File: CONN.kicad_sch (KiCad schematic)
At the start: 21 parts

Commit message: Complete schematics
Nightly update
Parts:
- removed D? (x15): LESD11LL5.0CT5G, 002_GN_TWO-PIN_PLASTIC_SMD:SOD-123, symbol 002_Basic_SingleSemiconductor:007_Diode_ESD_Bi
- added C25: 100nF, 001_GN_RCL_SMD:C0201(0603M), symbol 001_Basic_PassiveComponents:101_Capacitor
- added C26: 1uF, 001_GN_RCL_SMD:C0402(1005M), symbol 001_Basic_PassiveComponents:101_Capacitor
- added D10, D11, D12, D13, D14, D15, D16, D17, D3, D4, D5, D6, D7, D8, D9: LESD11LL5.0CT5G, 002_GN_TWO-PIN_PLASTIC_SMD:DFN-2_0603, symbol 002_Basic_SingleSemiconductor:007_Diode_ESD_Bi
- added J2, J6: Conn_01x04, symbol 302_Link_W2B-Connector:Conn_01x04
- added J4, J5: Conn_01x02, symbol 302_Link_W2B-Connector:Conn_01x02
- added Q1: YJL2101W, 003_GN_SMALL-SEMI_SMD:SOT-323, symbol 002_Basic_SingleSemiconductor:202_MOSFET_P-ch
- added Q2: TPM7002DFN3, 003_GN_SMALL-SEMI_SMD:DFN-3_1006, symbol 002_Basic_SingleSemiconductor:201_MOSFET_N-ch
- added R19: 10k, 001_GN_RCL_SMD:R0201(0603M), symbol 001_Basic_PassiveComponents:001_Resistor
- added U11: AW33901FCR, 104_SP_SMALL_SMD:LGA-9_1212_LSW, symbol 110_IntegratedCircuit_Interface:AW33901FCR
- D2: renamed from D?; footprint 002_GN_TWO-PIN_PLASTIC_SMD:SOD-123 -> 002_GN_TWO-PIN_PLASTIC_SMD:DFN-2_0603
- gave numbers to parts that had none: 5
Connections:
- net +3V3: now also J2.1, J6.1
- net DAP_CLK: now also D6.1 (Cathode)
- net DAP_DIO: now also D5.1 (Cathode)
- net DAP_Rx: now also D3.1 (Cathode)
- net DAP_Tx: now also D4.1 (Cathode)
- net DBG-RxN: now also D11.1 (Cathode)
- net DBG-RxP: now also D10.1 (Cathode)
- net DN: now also D8.1 (Cathode)
- net DP: now also D7.1 (Cathode)
- net DVC-DN: now also D17.1 (Cathode)
- net DVC-DP: now also D16.1 (Cathode)
- net GND: now also C25.2, C26.2, D10.2 (Anode), D11.2 (Anode), D12.2 (Anode), D13.2 (Anode), D14.2 (Anode), D15.2 (Anode), D16.2 (Anode), D17.2 (Anode), D3.2 (Anode), D4.2 (Anode), D5.2 (Anode), D6.2 (Anode), D7.2 (Anode), D8.2 (Anode), D9.2 (Anode), J2.4, J5.2, J6.4, Q2.2 (Source), U11.A1 (GND), U11.C1 (OV_FB)
- net SWCLK_TCK: now also J6.3
- net SWD-SBU1: now also D12.1 (Cathode)
- net SWD-SBU2: now also D13.1 (Cathode)
- net SWDIO_TMS: now also J6.2
- net UART-CC1: now also D14.1 (Cathode)
- net UART-CC2: now also D15.1 (Cathode)
- net VBUS: now also C25.1, U11.Vin
- net VDC: now also D9.1 (Cathode), Q1.2 (Source), R19.1
- new net: Q1.1 (Gate), Q2.3 (Drain), R19.2
- new net +5VP: C26.1, U11.Vout
- new net AUX_SWCLK: J2.3
- new net AUX_SWDIO: J2.2
- new net IDL-D: Q2.1 (Gate)
- new net KEY: J5.1
- new net SWRST_SRST: J4.1
- new net TRST: J4.2
- new net VDD: Q1.3 (Drain)
- no-connect marks 0 -> 1
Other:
- moved on the sheet: D2

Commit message: Nightly update
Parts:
- J2, J6: footprint (none) -> 251_CONN_PIN_HEADER_THD:VM-01x04_1mm
- J3: footprint (none) -> 206_CONN_USB:SCM-24_L1402ST
- J4, J5: footprint (none) -> 251_CONN_PIN_HEADER_THD:VM-01x02_1mm
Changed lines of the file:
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@@
     (property "Reference" "J5" (id 0) (at 45.72 171.45 0))
     (property "Value" "Conn_01x02" (id 1) (at 45.72 173.99 0))
-    (property "Footprint" "" (id 2) (at 45.72 177.8 0)
+    (property "Footprint" "251_CONN_PIN_HEADER_THD:VM-01x02_1mm" (id 2) (at 45.72 177.8 0)
       (effects (font (size 1.27 1.27)) hide)
     )
@@
       (effects (font (size 1.27 1.27)) (justify left))
     )
-    (property "Footprint" "" (id 2) (at 152.4 177.8 0)
+    (property "Footprint" "251_CONN_PIN_HEADER_THD:VM-01x02_1mm" (id 2) (at 152.4 177.8 0)
       (effects (font (size 1.27 1.27)) hide)
     )
@@
       (effects (font (size 1.27 1.27)) (justify left))
     )
-    (property "Footprint" "" (id 2) (at 81.28 176.53 0)
+    (property "Footprint" "251_CONN_PIN_HEADER_THD:VM-01x04_1mm" (id 2) (at 81.28 176.53 0)
       (effects (font (size 1.27 1.27)) hide)
     )
@@
     (property "Reference" "J2" (id 0) (at 99.06 168.91 0))
     (property "Value" "Conn_01x04" (id 1) (at 99.06 171.45 0))
-    (property "Footprint" "" (id 2) (at 99.06 176.53 0)
+    (property "Footprint" "251_CONN_PIN_HEADER_THD:VM-01x04_1mm" (id 2) (at 99.06 176.53 0)
       (effects (font (size 1.27 1.27)) hide)
     )
@@
     (property "Reference" "J3" (id 0) (at 190.5 44.45 0))
     (property "Value" "USB_TypeC-24" (id 1) (at 190.5 46.99 0))
-    (property "Footprint" "" (id 2) (at 190.5 45.72 0)
-      (effects (font (size 1.27 1.27)) hide)
-    )
+    (property "Footprint" "206_CONN_USB:SCM-24_L1402ST" (id 2) (at 190.5 45.72 0)
+      (effects (font (size 1.27 1.27)) hide)
+    )

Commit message: Complete package assignments
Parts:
- J1: footprint (none) -> 206_CONN_USB:SCF-24_7925SST
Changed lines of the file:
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@@
     (property "Reference" "J1" (id 0) (at 73.66 36.83 0))
     (property "Value" "USB_TypeC-24" (id 1) (at 73.66 39.37 0))
-    (property "Footprint" "" (id 2) (at 73.66 38.1 0)
+    (property "Footprint" "206_CONN_USB:SCF-24_7925SST" (id 2) (at 73.66 38.1 0)
       (effects (font (size 1.27 1.27)) hide)
     )

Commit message: Update layout
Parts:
- J3: footprint 206_CONN_USB:SCM-24_L1402ST -> 206_CONN_USB:SCM-24_L1402SST
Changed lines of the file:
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@@
     (property "Reference" "J3" (id 0) (at 190.5 44.45 0))
     (property "Value" "USB_TypeC-24" (id 1) (at 190.5 46.99 0))
-    (property "Footprint" "206_CONN_USB:SCM-24_L1402ST" (id 2) (at 190.5 45.72 0)
+    (property "Footprint" "206_CONN_USB:SCM-24_L1402SST" (id 2) (at 190.5 45.72 0)
       (effects (font (size 1.27 1.27)) hide)
     )

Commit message: Nightly update
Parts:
- R18, R20: footprint 001_GN_RCL_SMD:R0201(0603M) -> 001_GN_RCL_SMD:R0402(1005M)
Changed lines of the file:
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@@
       (effects (font (size 1.27 1.27)) (justify left))
     )
-    (property "Footprint" "001_GN_RCL_SMD:R0201(0603M)" (id 2) (at 180.34 45.72 0)
+    (property "Footprint" "001_GN_RCL_SMD:R0402(1005M)" (id 2) (at 180.34 45.72 0)
       (effects (font (size 1.27 1.27)) hide)
     )
@@
       (effects (font (size 1.27 1.27)) (justify left))
     )
-    (property "Footprint" "001_GN_RCL_SMD:R0201(0603M)" (id 2) (at 210.82 45.72 0)
+    (property "Footprint" "001_GN_RCL_SMD:R0402(1005M)" (id 2) (at 210.82 45.72 0)
       (effects (font (size 1.27 1.27)) hide)
     )

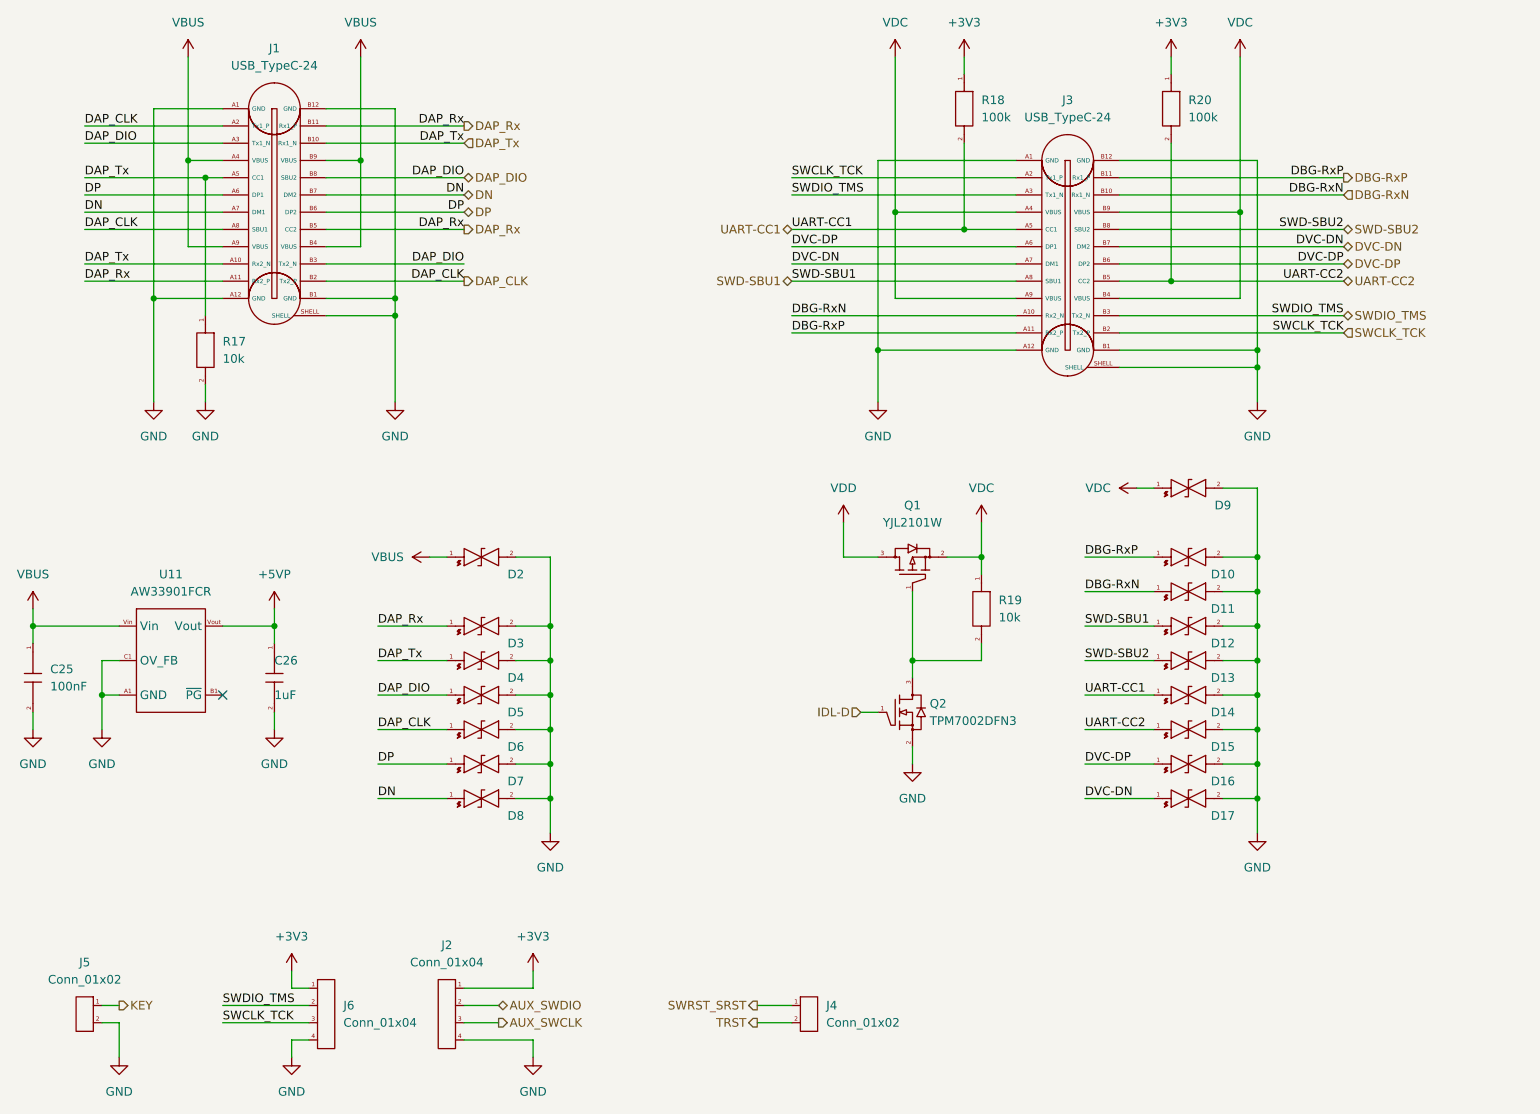
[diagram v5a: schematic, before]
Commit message: Correction line order of SCF CONN
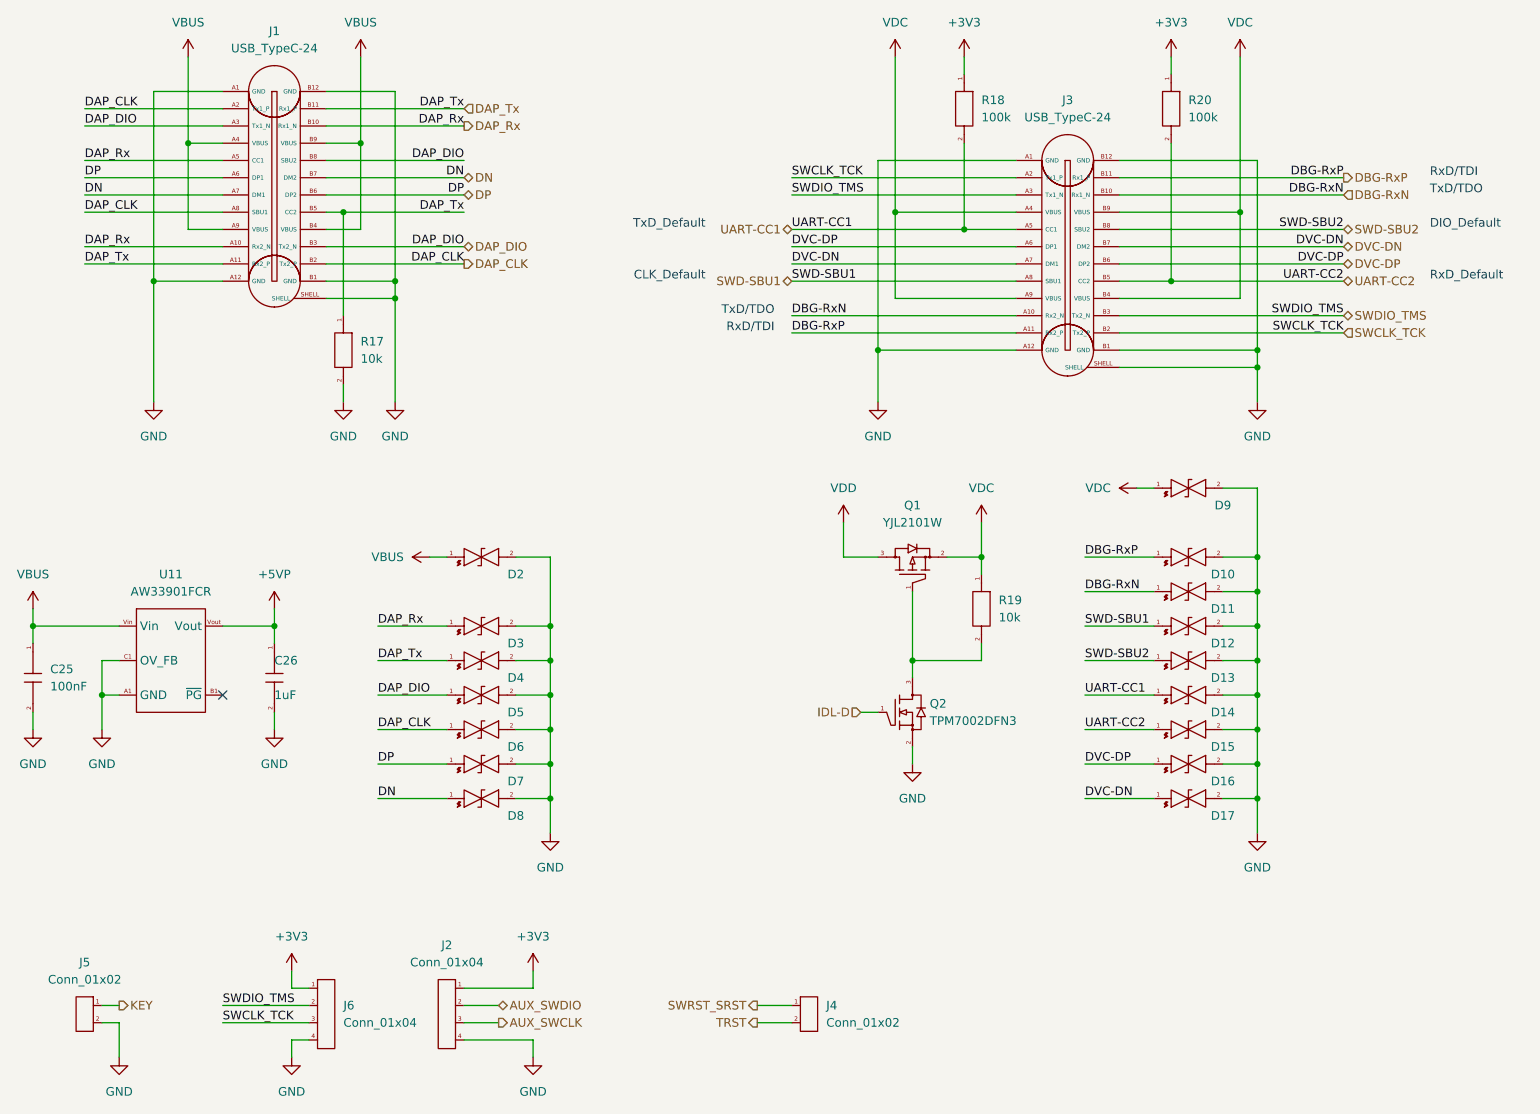
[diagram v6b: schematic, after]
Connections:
- net DAP_Rx: now also J1.A10 (Rx2_N), J1.A5 (CC1), J1.B10 (Rx1_N); no longer J1.A11 (Rx2_P), J1.B11 (Rx1_P), J1.B5 (CC2)
- net DAP_Tx: now also J1.A11 (Rx2_P), J1.B11 (Rx1_P), J1.B5 (CC2); no longer J1.A10 (Rx2_N), J1.A5 (CC1), J1.B10 (Rx1_N)
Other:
- note added: "CLK_Default"
- note added: "DIO_Default"
- note added: "RxD/TDI"
- note added: "RxD_Default"
- note added: "TxD/TDO"
- note added: "TxD_Default"
- moved on the sheet: J1, R17
